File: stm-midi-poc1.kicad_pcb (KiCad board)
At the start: 2 copper layers, 100 x 100 mm, 120 parts, among them CN1 MIDI Out 1, CN2 MIDI In 1, CN3 MIDI Out 2, CN4 MIDI In 2, CN5 Line out, CN6 Headphone, J1 GT-USB-7010I, J2 SWD, J3 I2C, J4 UART456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

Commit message: Move to 4 layer board; no other changes. S/G/S/G Top to Bottom.
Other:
- copper layers 2 -> 4
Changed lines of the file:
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@@
 	)
 	(layers
-		(0 "F.Cu" signal)
-		(31 "B.Cu" signal)
+		(0 "F.Cu" signal "F.Signal")
+		(1 "In1.Cu" power "F.GND")
+		(2 "In2.Cu" signal "B.Signal")
+		(31 "B.Cu" power "B.GND")
 		(32 "B.Adhes" user "B.Adhesive")
 		(33 "F.Adhes" user "F.Adhesive")
@@
 			)
 			(layer "dielectric 1"
-				(type "core")
-				(thickness 1.51)
+				(type "prepreg")
+				(thickness 0.1)
 				(material "FR4")
 				(epsilon_r 4.5)
+				(loss_tangent 0.02)
+			)
+			(layer "In1.Cu"
+				(type "copper")
+				(thickness 0.035)
+			)
+			(layer "dielectric 2"
+				(type "core")
+				(thickness 1.24)
+				(material "FR4")
+				(epsilon_r 4.5)
+				(loss_tangent 0.02)
+			)
+			(layer "In2.Cu"
+				(type "copper")
+				(thickness 0.035)
+			)
+			(layer "dielectric 3"
+				(type "prepreg")
+				(thickness 0.1)
+				(material "FR4")
+				(epsilon_r 4.5)

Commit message: Start routing through the new signal layer.
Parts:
- removed R32, R36: Zero, Resistor_SMD:R_2010_5025Metric
- removed R33, R34: Zero, Resistor_SMD:R_1206_3216Metric
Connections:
- CN6 pad 3: /User Interface/HPJ_R -> HEADPHONE_R
- SW2 pad 3: +3V3 -> +3.3VDAC
- SW3 pad 3: +3V3 -> +3.3VDAC
- U1 pad 25: /MCU/PIN_AM -> AUDIO_MUTE
- U1 pad 46: /MCU/PA13_SWDIO -> SYS_JTMS-SWDIO
- U3 pad 13: /Audio Output/HP_EN -> AUDIO_MUTE
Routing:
- net GND: track 362.4 -> 467.8 mm, vias 98 -> 109
- net USART2_RX: track 0.00 -> 45.5 mm, vias 0 -> 2
- net USART2_TX: track 0.00 -> 44.7 mm, vias 0 -> 2
- net HEADPHONE_R: track 15.2 -> 47.7 mm, vias 0 -> 2
- net /User Interface/HPJ_R: track 28.3 -> 0.00 mm
- net SYS_JTMS-SWDIO: track 51.5 -> 64.9 mm, vias 0 -> 2
- net AUDIO_MUTE: track 84.2 -> 96.8 mm, vias 0 -> 4
- net /MCU/PA13_SWDIO: track 11.9 -> 0.00 mm
- net LINE_R: track 55.5 -> 45.3 mm, vias 0 -> 2
- net +3.3VDAC: track 193.1 -> 184.7 mm, vias 0 -> 2
- net /Audio Output/HP_EN: track 5.63 -> 0.00 mm
- net /Audio Output/Gain0: track 70.3 -> 64.8 mm, vias 0 -> 2
- net /MCU/PIN_AM: track 4.89 -> 0.00 mm
- net USART3_TX: track 0.00 -> 3.08 mm, vias 0 -> 1
- net BTN2: track 38.7 -> 41.0 mm
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- added copper zone on In1.Cu, net GND

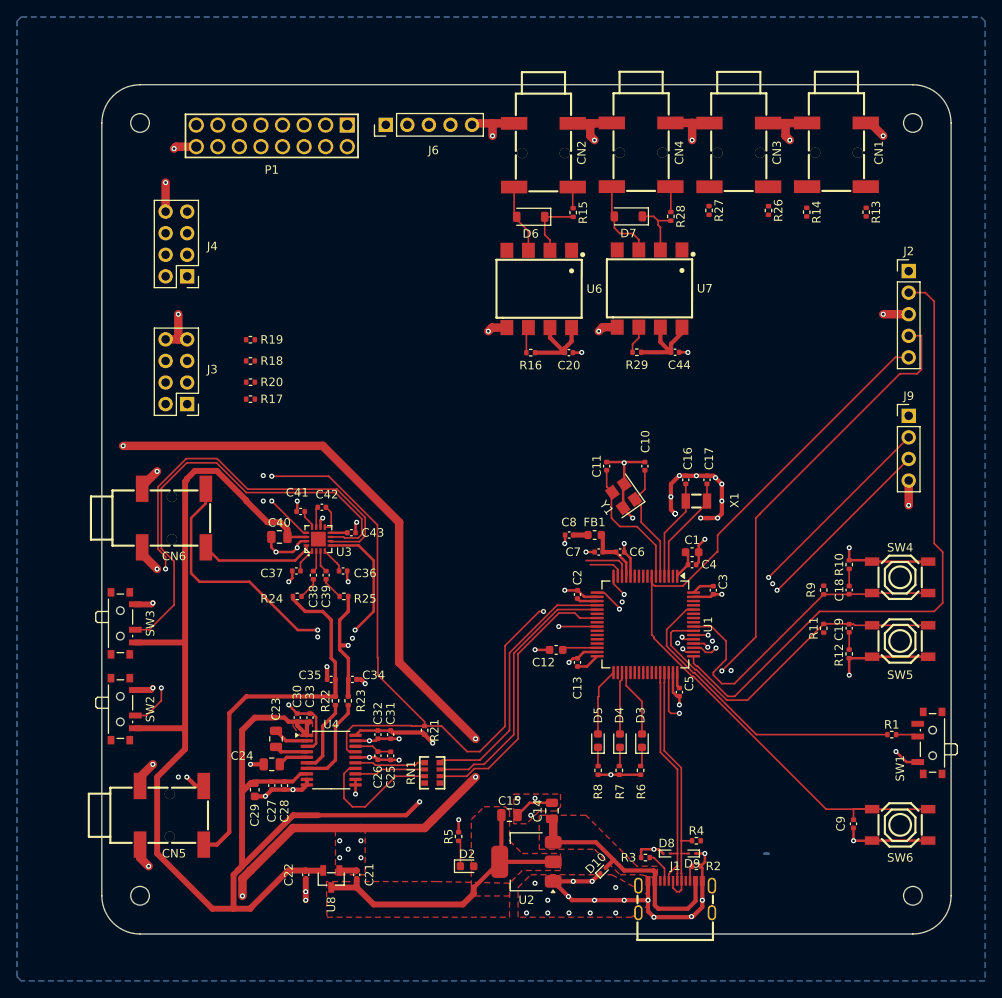
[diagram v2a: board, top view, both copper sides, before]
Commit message: Amateur hour. Routed all power and SPI, I2C, MIDI. Left GPIO and UARTs undone. Probably need to restart from scratch.
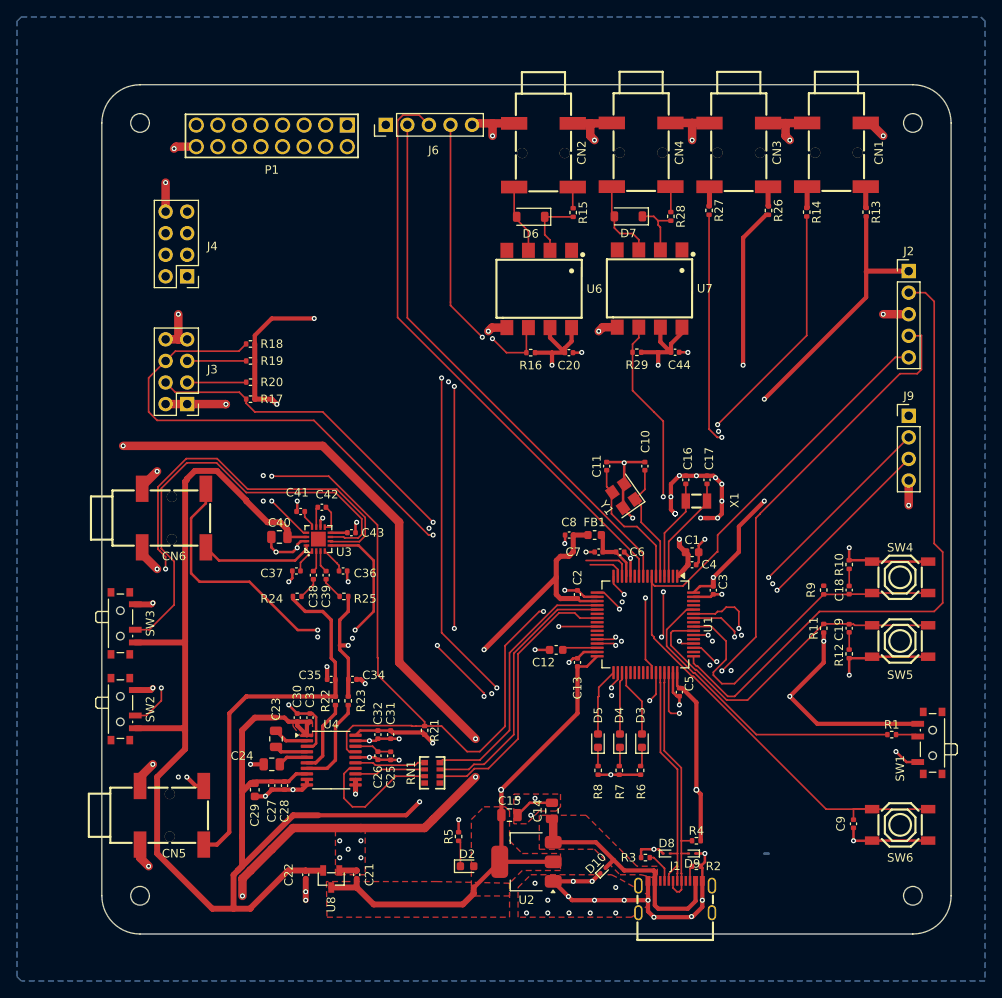
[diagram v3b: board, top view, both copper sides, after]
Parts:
- moved R19 2.50 mm to (124.5, 69.0)
- moved R18 2.00 mm to (124.5, 67.0)
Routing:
- net +3V3: track 72.1 -> 435.3 mm, vias 0 -> 15
- net I2C1_SDA: track 0.00 -> 92.8 mm, vias 0 -> 1
- net I2C1_SCL: track 0.00 -> 91.6 mm, vias 0 -> 1
- net SPI2_SCK: track 0.00 -> 88.1 mm, vias 0 -> 4
- net I2C2_SDA: track 0.00 -> 85.8 mm, vias 0 -> 2
- net USART1_RX: track 3.05 -> 78.5 mm, vias 0 -> 6
- net SPI2_MISO: track 0.00 -> 69.9 mm
- net I2C2_SCL: track 0.00 -> 68.0 mm, vias 0 -> 2
- net SPI2_MOSI: track 0.00 -> 64.7 mm
- net USART1_TX: track 0.00 -> 61.9 mm, vias 0 -> 2
- net USART3_TX: track 3.08 -> 63.5 mm, vias 1 -> 2
- net USART3_RX: track 5.11 -> 42.5 mm, vias 1 -> 4
- net GND: track 467.8 -> 483.5 mm, vias 109 -> 116
- net /MIDI/MO1-SRC: track 0.00 -> 2.51 mm
- net /MIDI/MO1-SNK: track 0.00 -> 2.51 mm
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
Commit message: Routed power to the GPIO/I2C
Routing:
- net +3V3: track 435.3 -> 512.1 mm
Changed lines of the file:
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@@
+	)
+	(segment
+		(start 117.04 51.42)
+		(end 117.04 48.04)
+		(width 1)
+		(layer "In2.Cu")
+		(net 2)
 	)
 	(segment
@@
 	)
 	(segment
+		(start 120.5 53)
+		(end 118.92 51.42)
+		(width 1)
+		(layer "In2.Cu")
+		(net 2)
+	)
+	(segment
+		(start 117.04 48.04)
+		(end 113.5 44.5)
+		(width 1)
+		(layer "In2.Cu")
+		(net 2)
+	)
+	(segment
+		(start 113.5 44.5)
+		(end 113.5 44)
+		(width 1)
+		(layer "In2.Cu")
+		(net 2)
+	)
+	(segment
+		(start 111.5 63)
+		(end 112.5 62)
+		(width 1)
+		(layer "In2.Cu")
+		(net 2)
+	)
+	(segment
 		(start 152 103)
 		(end 149 106)
@@
 	)
 	(segment
+		(start 114.5 74.08)
+		(end 111.58 74.08)
+		(width 1)
+		(layer "In2.Cu")
+		(net 2)
+	)
+	(segment
+		(start 137.7262 38.5)
+		(end 140.425 41.1988)
+		(width 1)
+		(layer "In2.Cu")
+		(net 2)
+	)
+	(segment
 		(start 154 119.5)
 		(end 177 119.5)
@@
 	)
 	(segment
+		(start 118.11 39.39)
+		(end 119 38.5)
+		(width 1)
+		(layer "In2.Cu")
+		(net 2)
+	)
+	(segment
 		(start 175 90.5)
 		(end 175 90)
@@
 	)
 	(segment
+		(start 119 38.5)
+		(end 137.7262 38.5)
+		(width 1)
+		(layer "In2.Cu")
+		(net 2)
+	)
+	(segment
 		(start 121.601727 74.102536)
 		(end 127.600109 74.102536)
@@
 	)
 	(segment
+		(start 118.11 41.23)
+		(end 118.11 39.39)
+		(width 1)
+		(layer "In2.Cu")
+		(net 2)
+	)
+	(segment
+		(start 120.5 62)
+		(end 120.5 53)
+		(width 1)
+		(layer "In2.Cu")
+		(net 2)
+	)
+	(segment
+		(start 111.58 74.08)
+		(end 111.5 74)
+		(width 1)
+		(layer "In2.Cu")
+		(net 2)
+	)
+	(segment
 		(start 185 85.5)
 		(end 185 75.5)
@@
 	)
 	(segment
+		(start 116.27 41.23)
+		(end 118.11 41.23)
+		(width 1)
+		(layer "In2.Cu")
+		(net 2)
+	)
+	(segment
 		(start 185 72)
 		(end 182.5 69.5)
@@
 	)
 	(segment
+		(start 113.5 44)
+		(end 116.27 41.23)
+		(width 1)
+		(layer "In2.Cu")
+		(net 2)
+	)
+	(segment
 		(start 185.04 75.46)
 		(end 185 75.5)
@@
 	)
 	(segment
+		(start 112.5 62)
+		(end 120.5 62)
+		(width 1)
+		(layer "In2.Cu")
+		(net 2)
+	)
+	(segment
+		(start 118.92 51.42)
+		(end 117.04 51.42)
+		(width 1)
+		(layer "In2.Cu")
+		(net 2)
+	)
+	(segment
 		(start 179 94.5)
 		(end 175 90.5)
@@
 		(layer "In2.Cu")
 		(net 2)
+	)
+	(segment
+		(start 111.5 74)
+		(end 111.5 63)
+		(width 1)
+		(layer "In2.Cu")
+		(net 2)

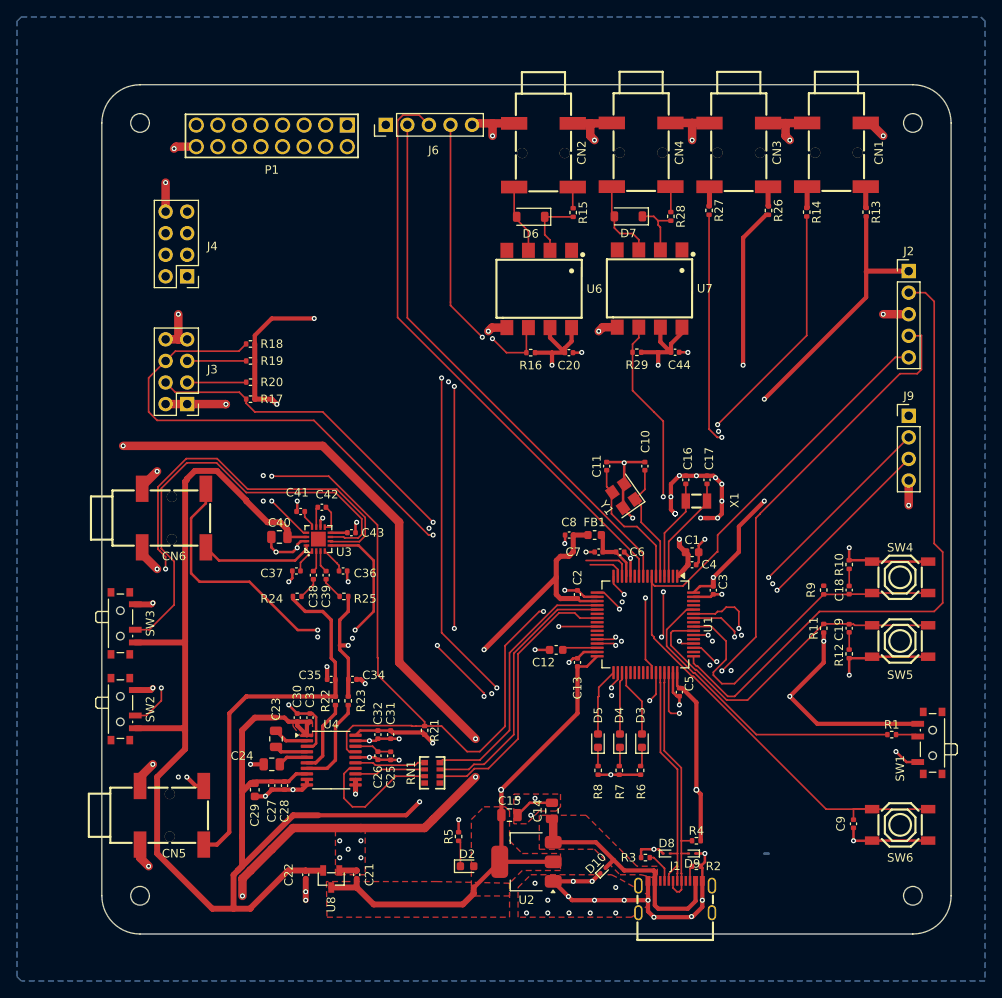
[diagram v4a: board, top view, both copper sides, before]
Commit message: Removed all vias/tracks and moved signal layers to outside for this EVT board design
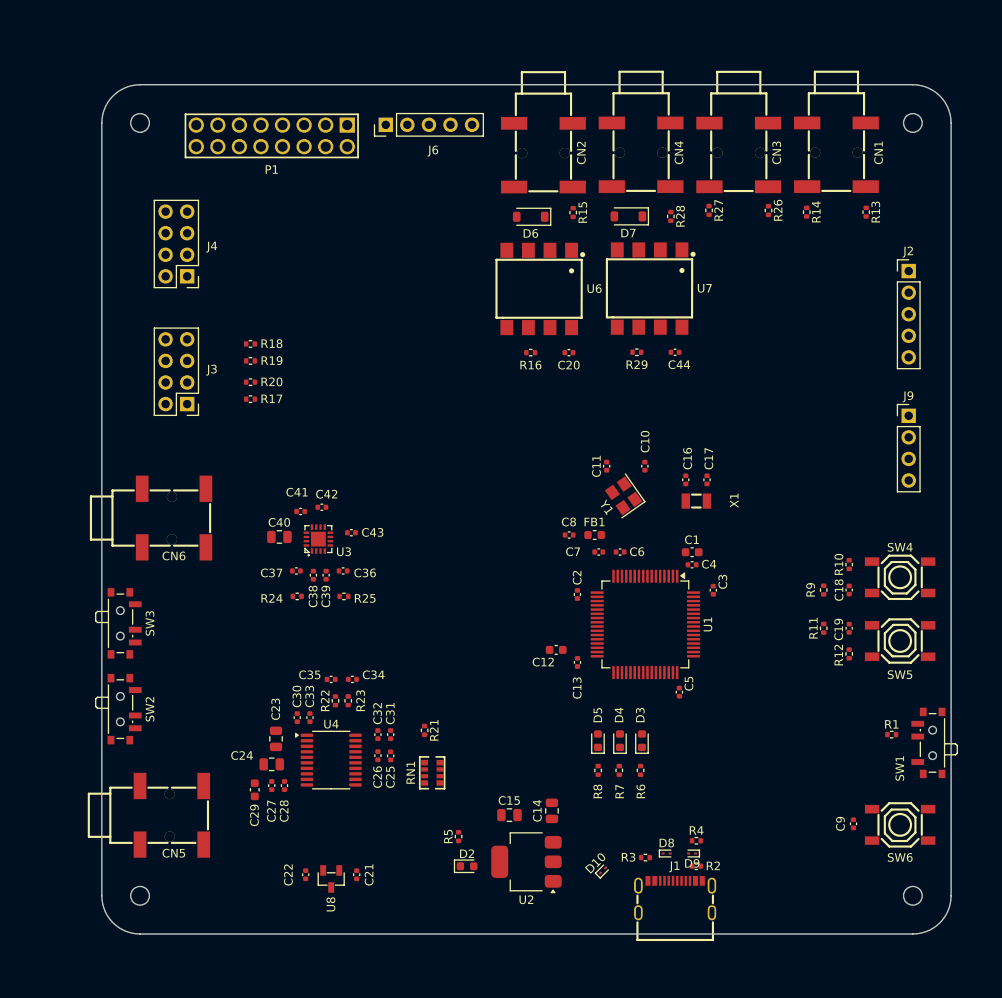
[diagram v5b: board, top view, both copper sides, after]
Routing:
- net +3V3: track 512.1 -> 0.00 mm, vias 15 -> 0
- net GND: track 483.5 -> 0.00 mm, vias 116 -> 0
- net +3.3VDAC: track 184.7 -> 0.00 mm, vias 2 -> 0
- net AUDIO_MUTE: track 96.8 -> 0.00 mm, vias 4 -> 0
- net NRST: track 95.0 -> 0.00 mm
- net I2C1_SDA: track 92.8 -> 0.00 mm, vias 1 -> 0
- net I2C1_SCL: track 91.6 -> 0.00 mm, vias 1 -> 0
- net SPI2_SCK: track 88.1 -> 0.00 mm, vias 4 -> 0
- net I2C2_SDA: track 85.8 -> 0.00 mm, vias 2 -> 0
- net USART1_RX: track 78.5 -> 0.00 mm, vias 6 -> 0
- net SYS_JTCK-SWCLK: track 75.7 -> 0.00 mm
- net SPI2_MISO: track 69.9 -> 0.00 mm
- net I2C2_SCL: track 68.0 -> 0.00 mm, vias 2 -> 0
- net SYS_JTMS-SWDIO: track 64.9 -> 0.00 mm, vias 2 -> 0
- net /Audio Output/Gain0: track 64.8 -> 0.00 mm, vias 2 -> 0
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- removed copper zone on F.Cu, net +3.3VDAC
- removed copper zone on F.Cu, net +3V3
- removed copper zone on B.Cu, net GND
- removed copper zone on F.Cu, net GND
- removed copper zone on In1.Cu, net GND
- removed copper zone on F.Cu, net VBUS

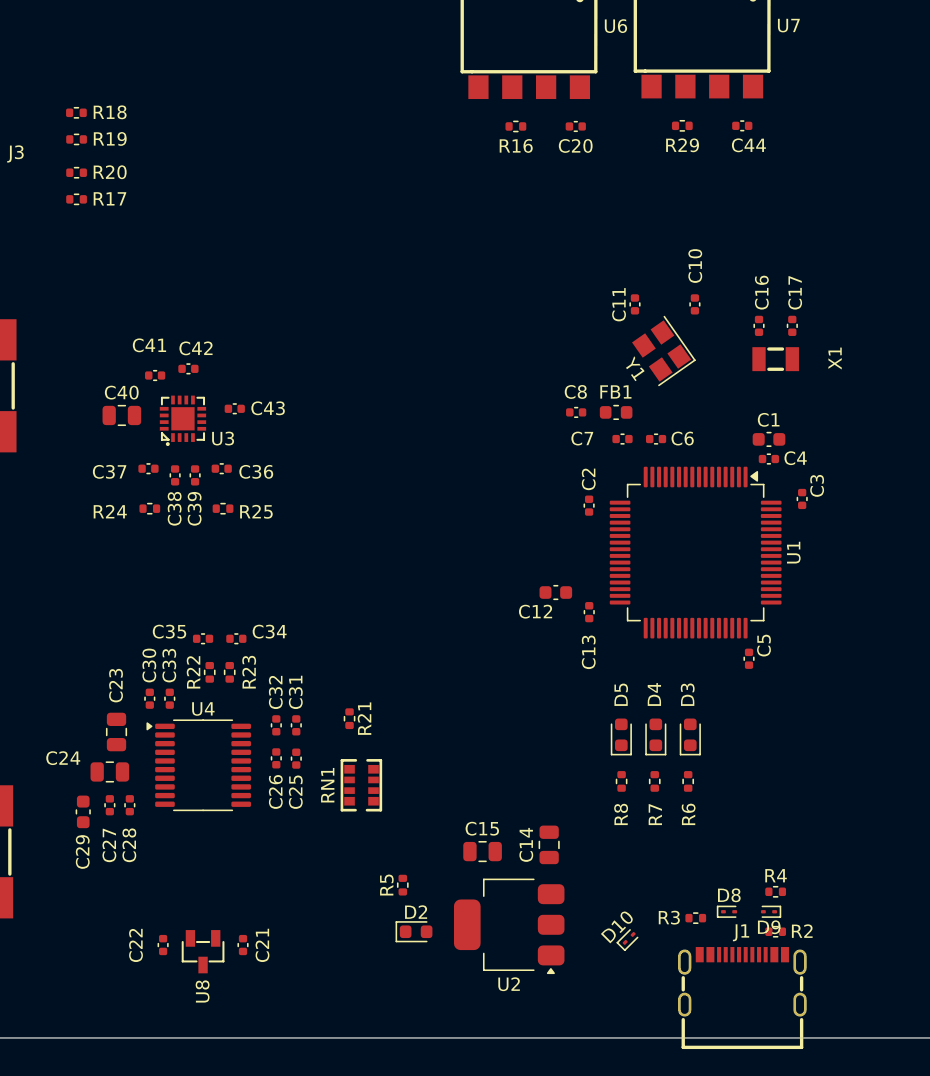
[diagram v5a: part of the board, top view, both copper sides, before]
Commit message: Routed all decoupling caps on top layer, as well as USB power input.
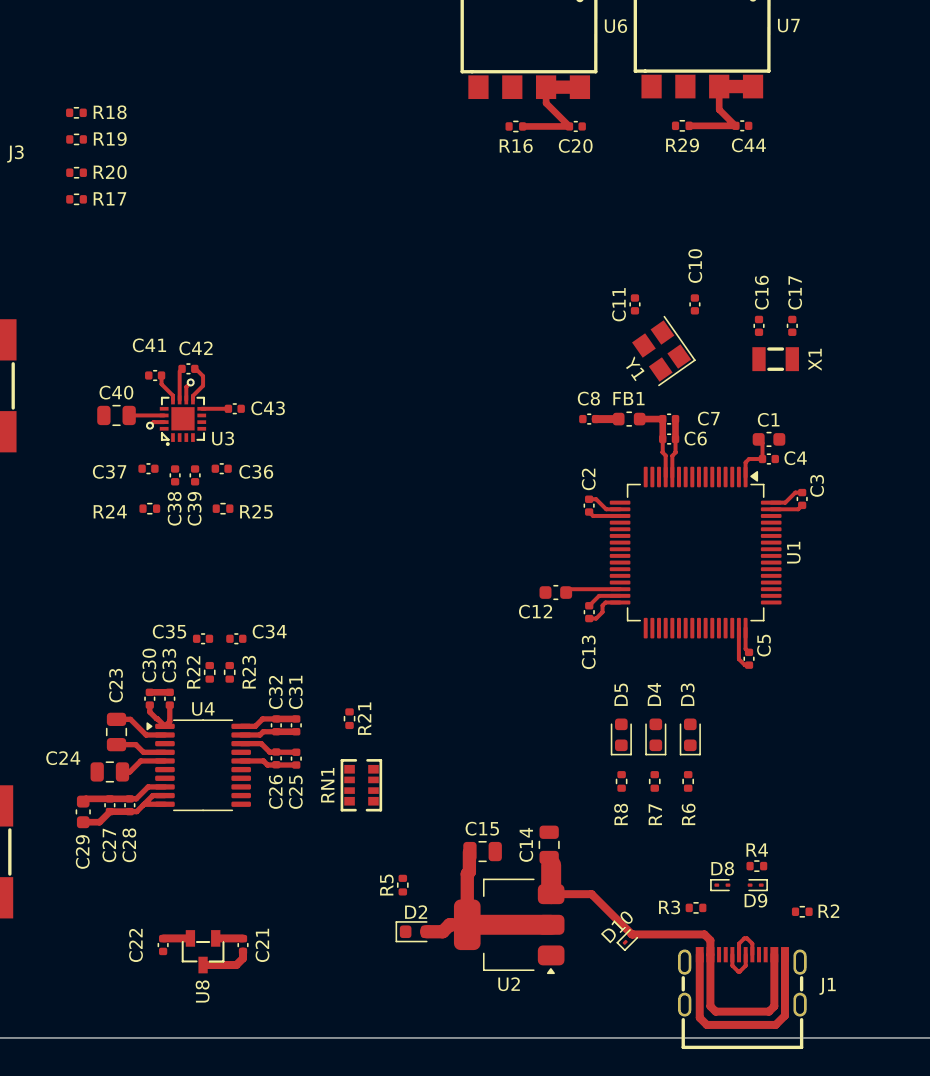
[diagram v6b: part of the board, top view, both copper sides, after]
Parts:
- moved C7 3.81 mm to (169.0, 90.0), turned to 0 degrees
- moved R2 2.50 mm to (179.0, 127.0)
- moved R4 2.39 mm to (175.6, 123.6)
- moved D9 2.24 mm to (175.5, 125.0)
- moved D8 2.06 mm to (173.0, 125.0)
- moved C8 1.10 mm to (163.0, 90.0)
- moved FB1 1.10 mm to (166.0, 90.0)
- moved C6 0.98 mm to (169.0, 91.5)
- moved R3 0.77 mm to (171.0, 126.7)
- moved C40 0.40 mm to (127.5, 89.7)
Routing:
- net GND: track 0.00 -> 55.0 mm, vias 0 -> 2
- net +3V3: track 0.00 -> 54.1 mm
- net VBUS: track 0.00 -> 29.5 mm
- net +3.3VDAC: track 0.00 -> 19.1 mm
- net +3V3A: track 0.00 -> 6.19 mm
- net /Audio Output/DAC_LDOO: track 0.00 -> 4.40 mm
- net /MCU/VCAP_1: track 0.00 -> 4.15 mm
- net /Audio Output/DAC_CAPP: track 0.00 -> 4.12 mm
- net /Audio Output/DAC_CAPM: track 0.00 -> 3.88 mm
- net /Audio Output/DAC_VNEG: track 0.00 -> 3.53 mm
- net /MCU/USB_OTG_FS_D-: track 0.00 -> 3.02 mm
- net /MCU/USB_OTG_FS_D+: track 0.00 -> 2.98 mm
- net /Audio Output/HPA_CAP-: track 0.00 -> 2.80 mm
- net /Audio Output/HPA_CAP+: track 0.00 -> 2.41 mm
- net /Audio Output/HPA_HPVDD: track 0.00 -> 2.20 mm
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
